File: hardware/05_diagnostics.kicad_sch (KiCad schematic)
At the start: 12 parts, among them J8 UPDI / AUX / GND, SW1 TL3340AF160QG, U10 ATTINY1616-SNR

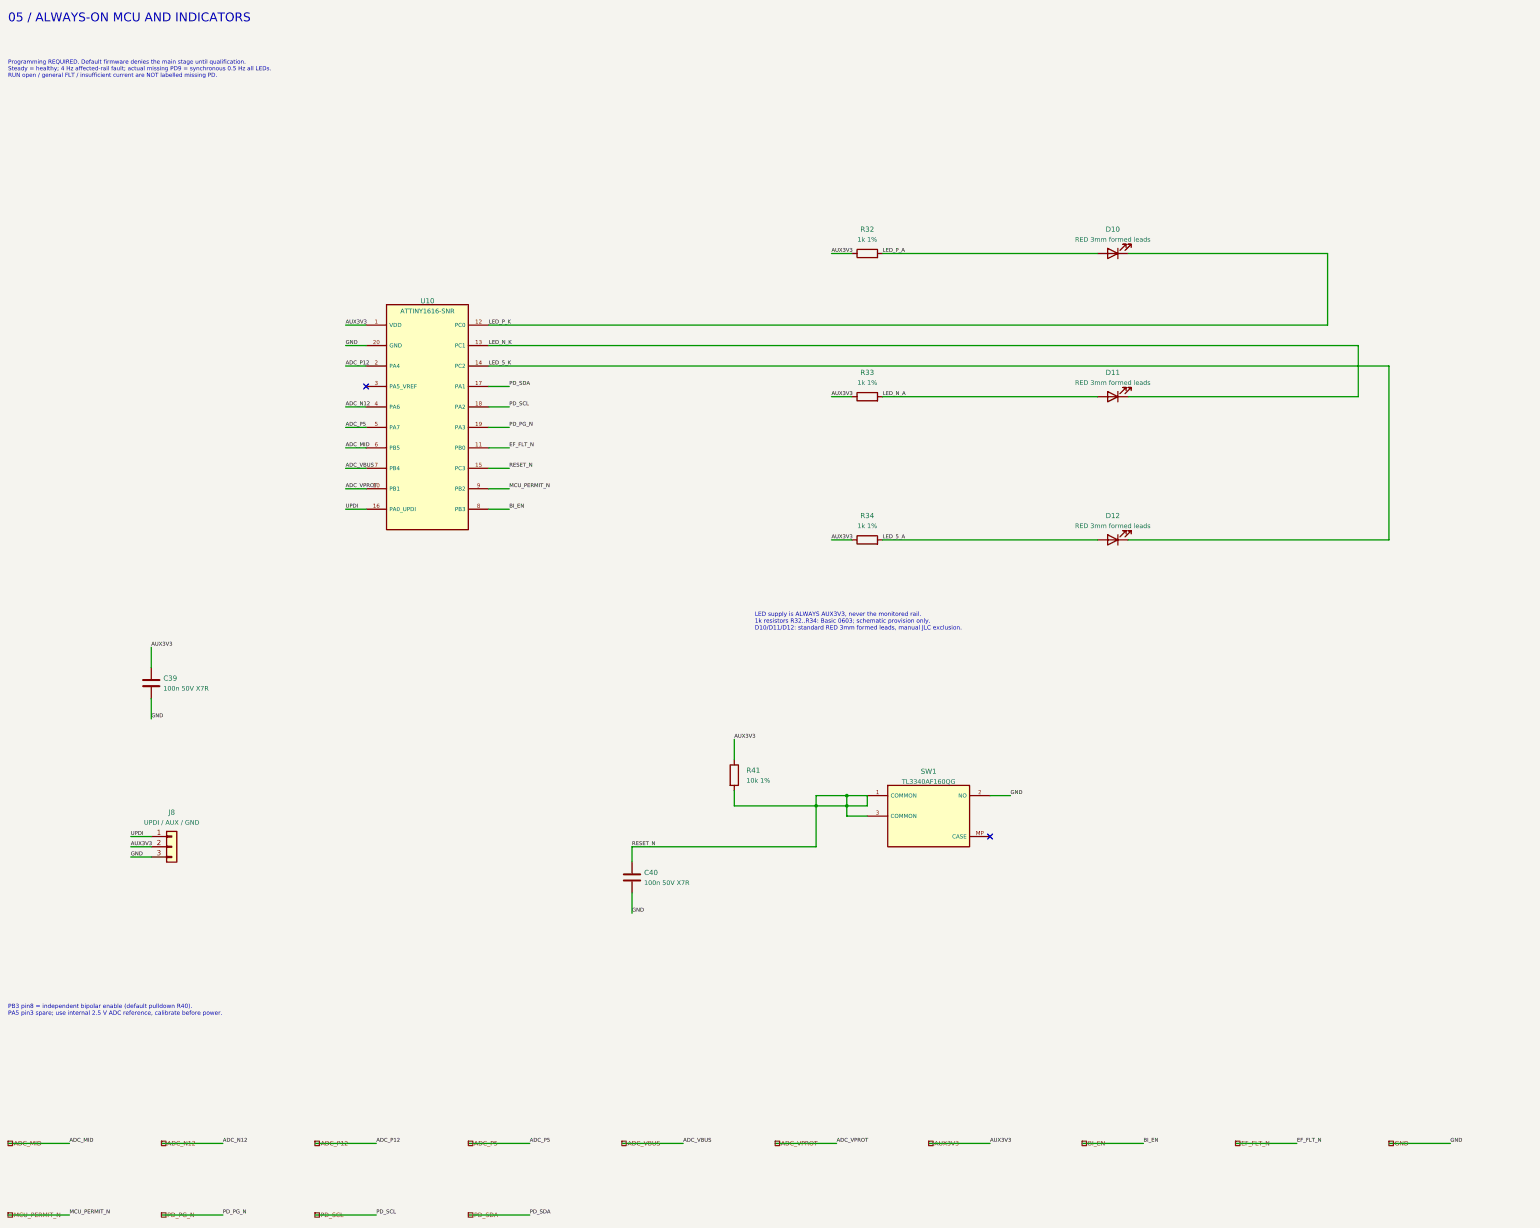
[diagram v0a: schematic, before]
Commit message: Replace MCU diagnostics with optional rail-sense IDC and single 5 V power LED
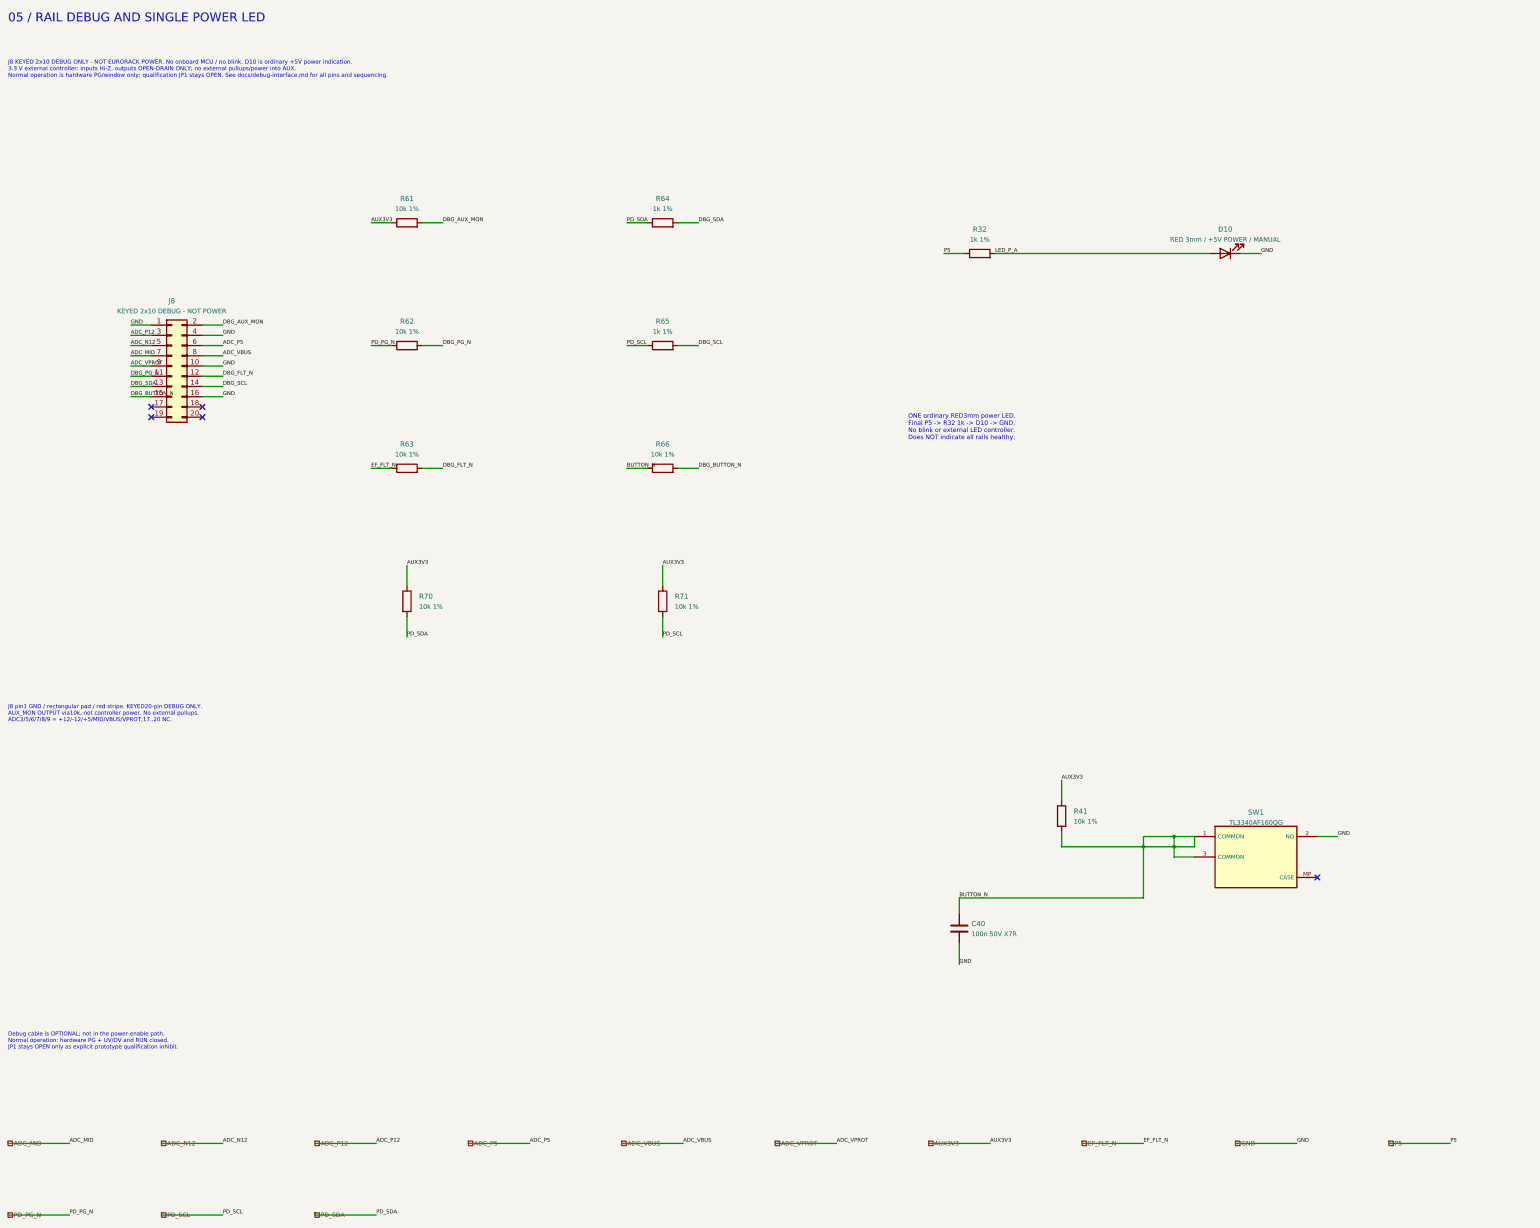
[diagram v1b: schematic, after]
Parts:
- removed C39: 100n 50V X7R, BigModular:C_0603_1608Metric, symbol BigModular:Device_C
- removed D11, D12: RED 3mm formed leads, BigModular:LED_D3.0mm_Horizontal_O1.27mm_Z2.0mm_Edge, symbol BigModular:Device_LED
- removed R33, R34: 1k 1%, BigModular:R_0603_1608Metric, symbol BigModular:Device_R
- removed U10: ATTINY1616-SNR, BigModular:SOIC-20W_7.5x12.8mm_P1.27mm, symbol BigModular:ATTINY1616_SNR
- added R61, R62, R63, R66, R70, R71: 10k 1%, BigModular:R_0603_1608Metric, symbol BigModular:Device_R
- added R64, R65: 1k 1%, BigModular:R_0603_1608Metric, symbol BigModular:Device_R
- D10: value RED 3mm formed leads -> RED 3mm / +5V POWER / MANUAL; NOTE Hand solder standard3mm LED, no proprietary holder; cathode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 -> Single hand-soldered red3mm power LED: P5 -> R32 1k -> anod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
- J8: value UPDI / AUX / GND -> KEYED 2x10 DEBUG - NOT POWER; footprint BigModular:PinHeader_1x03_P2.54mm_Vertical -> BigModular:IDC-Header_2x10_P2.54mm_Vertical; symbol BigModular:Connector_Generic_Conn_01x03 -> BigModular:Connector_Generic_Conn_02x10_Odd_Even; NOTE Programming pads/header provision. Do not backpower VBUS; p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 -> Replaces old 3-pin UPDI. Keyed 20-pin debug IDC; pin1 recta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
- R32: NOTE Prototype candidate; qualify ratings, land pattern and oper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 -> Ordinary final +5V power indicator only: 1k series limits c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
- SW1: NOTE P021301 Rev B: contacts1+3 common RESET_N, contact2 GND; du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 -> P021301 Rev B: contacts1+3 common BUTTON_N, contact2 GND; d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
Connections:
- net LED_P_K is gone; now on net GND: D10.1 (K)
- net UPDI is gone; now on net GND: J8.1 (Pin_1)
- net ADC_MID: now also J8.7 (Pin_7)
- net ADC_N12: now also J8.5 (Pin_5)
- net ADC_P12: now also J8.3 (Pin_3)
- net ADC_P5: now also J8.6 (Pin_6)
- net ADC_VBUS: now also J8.8 (Pin_8)
- net ADC_VPROT: now also J8.9 (Pin_9)
- net AUX3V3: now also R61.1, R70.1, R71.1; no longer J8.2 (Pin_2), R32.1
- net EF_FLT_N: now also R63.1
- net GND: now also J8.10 (Pin_10), J8.16 (Pin_16), J8.4 (Pin_4); no longer J8.3 (Pin_3)
- net PD_PG_N: now also R62.1
- net PD_SCL: now also R65.1, R71.2
- net PD_SDA: now also R64.1, R70.2
- net RESET_N renamed BUTTON_N
- net BUTTON_N: now also R66.1
- new net DBG_AUX_MON: J8.2 (Pin_2), R61.2
- new net DBG_BUTTON_N: J8.15 (Pin_15), R66.2
- new net DBG_FLT_N: J8.12 (Pin_12), R63.2
- new net DBG_PG_N: J8.11 (Pin_11), R62.2
- new net DBG_SCL: J8.14 (Pin_14), R65.2
- new net DBG_SDA: J8.13 (Pin_13), R64.2
- new net P5: R32.1
- no-connect marks 2 -> 5
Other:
- note added: "05 / RAIL DEBUG AND SINGLE POWER LED"
- note added: "Debug cable is OPTIONAL; not in the power-enable path. Normal operation: hardware PG + UV/OV and RUN closed. JP1 stays OPEN only as explicit prototype qualification inhibit."
- note added: "J8 KEYED 2x10 DEBUG ONLY - NOT EURORACK POWER. No onboard MCU / no blink. D10 is ordinary +5V power indication. 3.3 V external controller: inputs Hi-Z, outputs OPEN-DRAIN ONLY; no external pullups/power into AUX. Normal operation is hardware PG/window only; qualification JP1 stays OPEN. See docs/debug-interface.md for all pins and sequencing."
- note added: "J8 pin1 GND / rectangular pad / red stripe. KEYED20-pin DEBUG ONLY. AUX_MON OUTPUT via10k, not controller power. No external pullups. ADC3/5/6/7/8/9 = +12/-12/+5/MID/VBUS/VPROT;17..20 NC."
- note added: "ONE ordinary RED3mm power LED. Final P5 -> R32 1k -> D10 -> GND. No blink or external LED controller. Does NOT indicate all rails healthy."
- note removed: "05 / ALWAYS-ON MCU AND INDICATORS"
- note removed: "LED supply is ALWAYS AUX3V3, never the monitored rail. 1k resistors R32..R34: Basic 0603; schematic provision only. D10/D11/D12: standard RED 3mm formed leads, manual JLC exclusion."
- note removed: "PB3 pin8 = independent bipolar enable (default pulldown R40). PA5 pin3 spare; use internal 2.5 V ADC reference, calibrate before power."
- note removed: "Programming REQUIRED. Default firmware denies the main stage until qualification. Steady = healthy; 4 Hz affected-rail fault; actual missing PD9 = synchronous 0.5 Hz all LEDs. RUN open / general FLT / insufficient current are NOT labelled missing PD."
- title: Big Modular - Always-on MCU and indicators -> Big Modular - Rail debug and single power LED
- moved on the sheet: C40, D10, R32, R41, SW1

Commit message: Clarify hierarchical ports and replace local label islands with visible schematic wiring
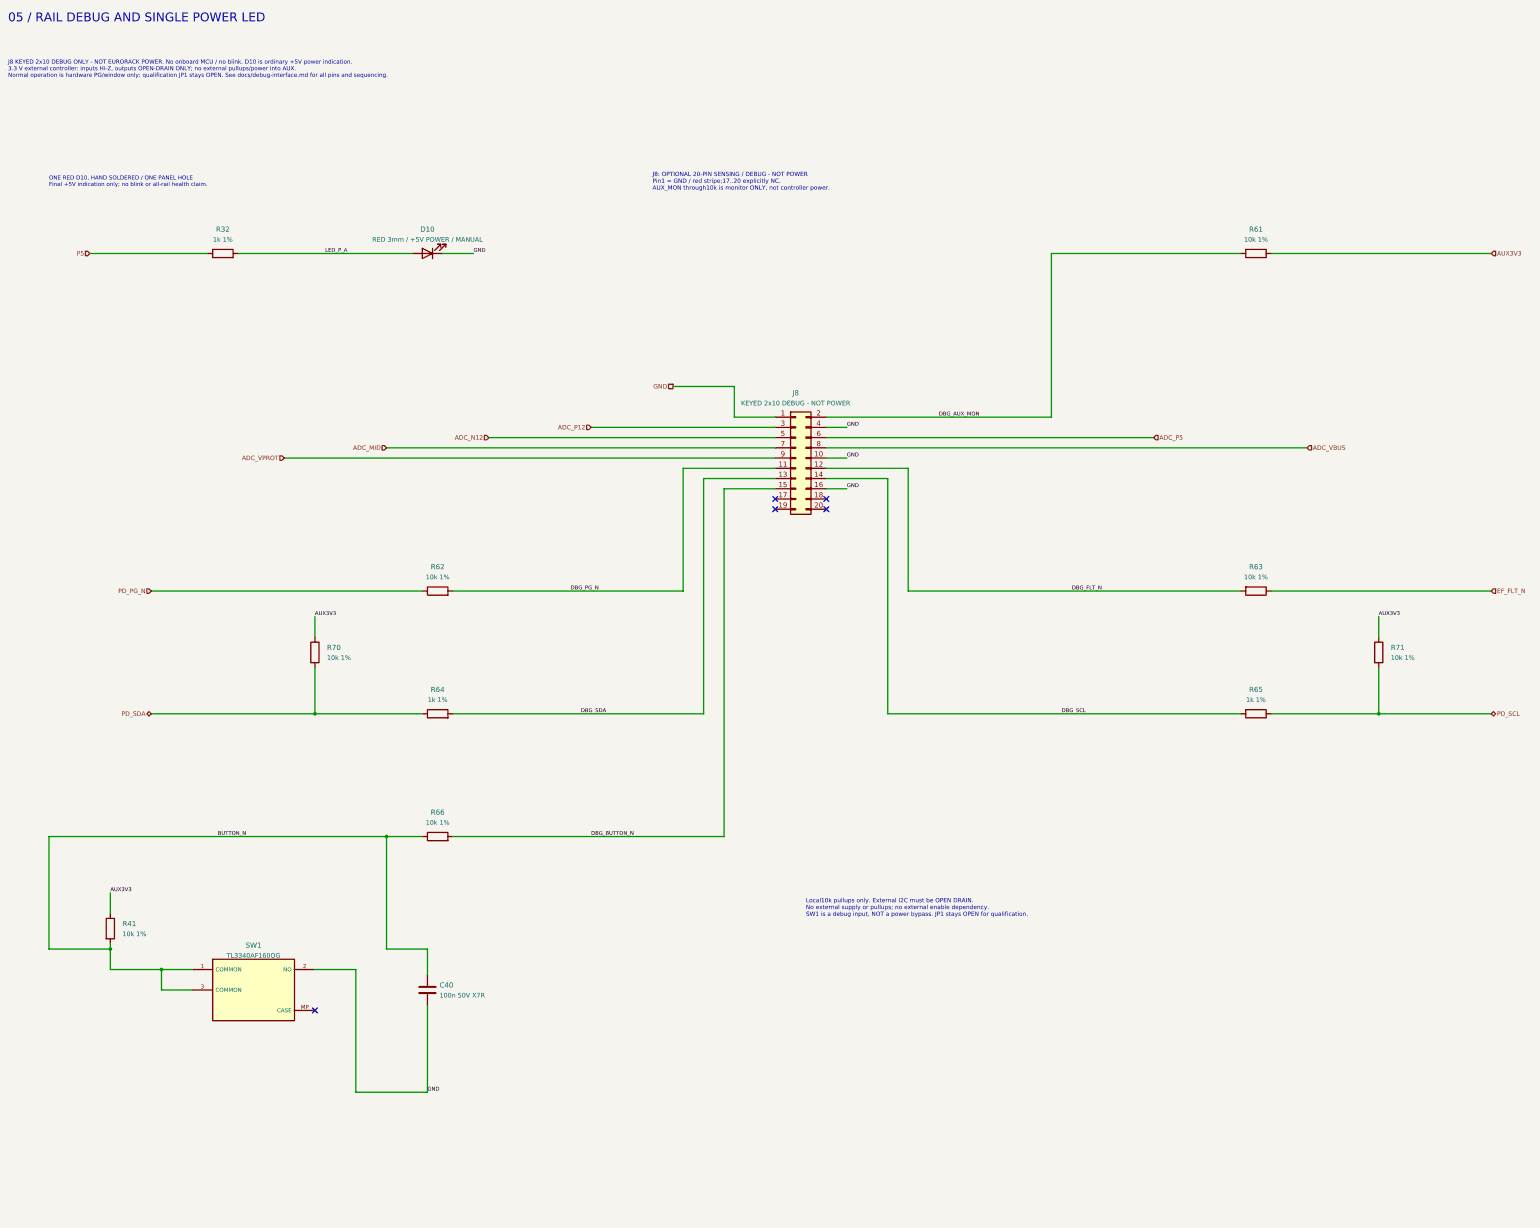
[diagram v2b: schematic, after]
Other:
- note added: "J8: OPTIONAL 20-PIN SENSING / DEBUG - NOT POWER Pin1 = GND / red stripe;17..20 explicitly NC. AUX_MON through10k is monitor ONLY, not controller power."
- note added: "Local10k pullups only. External I2C must be OPEN DRAIN. No external supply or pullups; no external enable dependency. SW1 is a debug input, NOT a power bypass. JP1 stays OPEN for qualification."
- note added: "ONE RED D10, HAND SOLDERED / ONE PANEL HOLE Final +5V indication only; no blink or all-rail health claim."
- note removed: "Debug cable is OPTIONAL; not in the power-enable path. Normal operation: hardware PG + UV/OV and RUN closed. JP1 stays OPEN only as explicit prototype qualification inhibit."
- note removed: "J8 pin1 GND / rectangular pad / red stripe. KEYED20-pin DEBUG ONLY. AUX_MON OUTPUT via10k, not controller power. No external pullups. ADC3/5/6/7/8/9 = +12/-12/+5/MID/VBUS/VPROT;17..20 NC."
- note removed: "ONE ordinary RED3mm power LED. Final P5 -> R32 1k -> D10 -> GND. No blink or external LED controller. Does NOT indicate all rails healthy."
- moved on the sheet: C40, D10, J8, R32, R41, R61, R62, R63, R64, R65, R66, R70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
